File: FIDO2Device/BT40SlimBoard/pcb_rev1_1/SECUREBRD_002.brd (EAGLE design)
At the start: 30 x 30 mm, 37 parts, among them CN1 USB4105-GF-A, CN2 IF_5PIN_H, CN3 IF_2PIN_SOL, SW1 SKRPACE010, SW2 SKTADAE010, U1 BT40, U2 ADP122ACPZ-3.3-R7, U3 RV-3028-C7

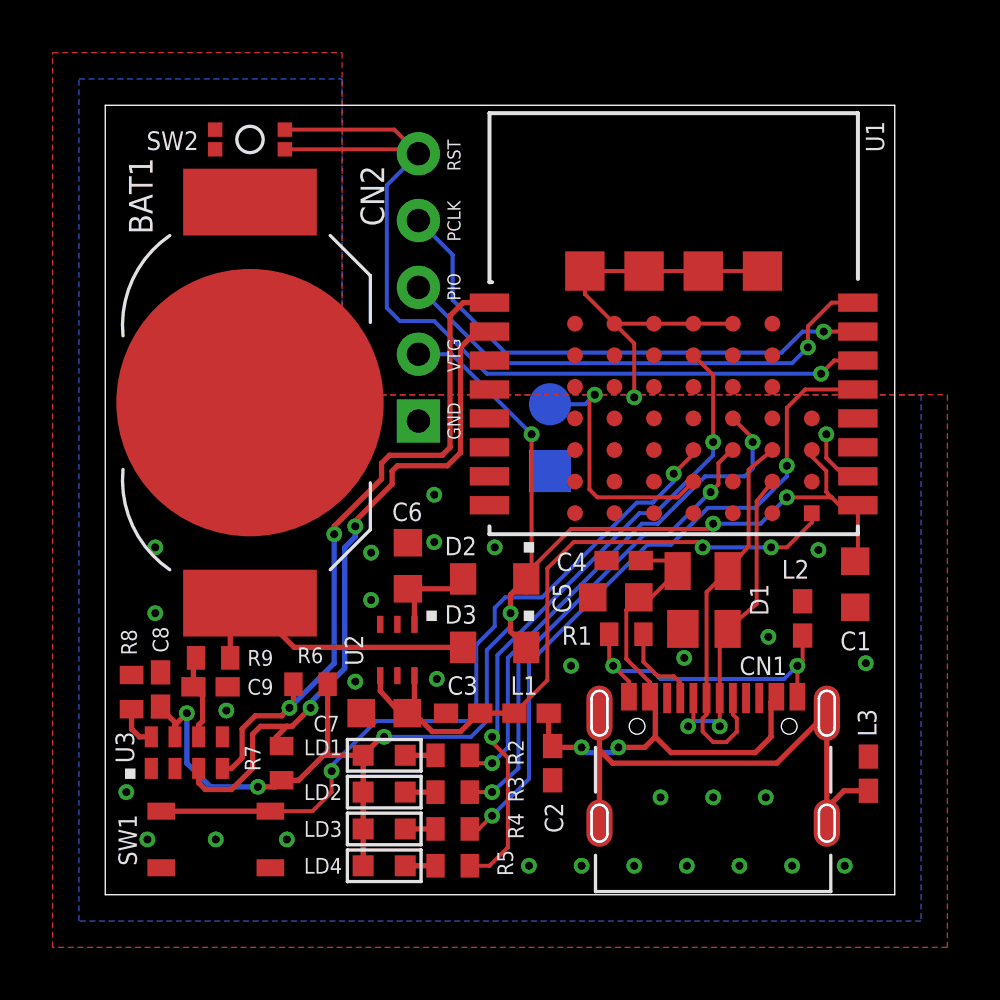
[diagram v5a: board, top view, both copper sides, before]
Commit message: 配線レイアウトを修正
・電池ホルダーの位置を微調整
・実装図面を修正
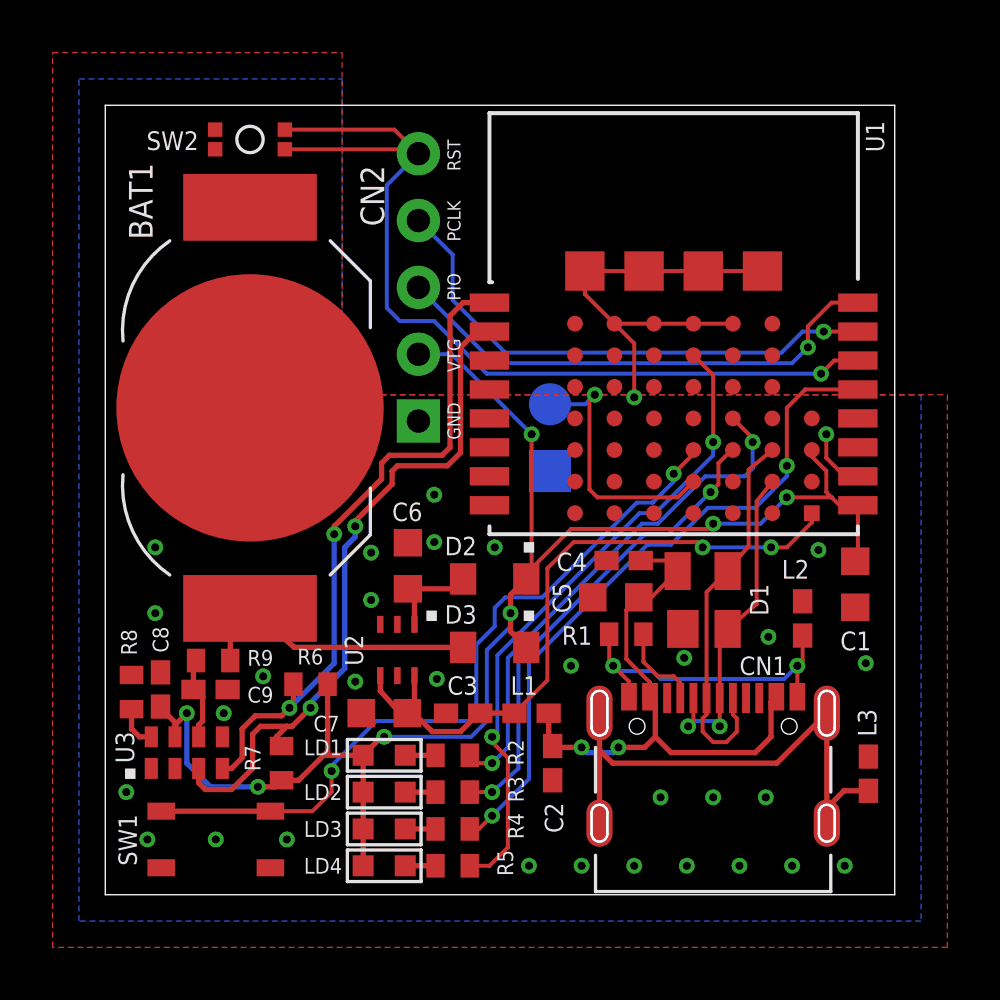
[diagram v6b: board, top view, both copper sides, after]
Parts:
- moved BAT1 0.20 mm to (5.50, 18.5)
- moved C9 0.10 mm to (4.00, 7.80)
- moved R9 0.10 mm to (4.10, 8.90)
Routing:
- net 0V: vias 31 -> 32
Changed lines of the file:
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@@
 <text x="15.8" y="18.6" size="0.6" layer="22" rot="MR270" align="bottom-center">TXD</text>
 <text x="15.8" y="16.1" size="0.6" layer="22" rot="MR270" align="bottom-center">GND</text>
+<dimension x1="0" y1="30" x2="30" y2="30" x3="15" y3="31.5" textsize="1.778" layer="51"/>
+<dimension x1="0" y1="0" x2="0" y2="30" x3="-1.5" y3="15" textsize="1.778" layer="51"/>
 </plain>
 <attributes>
@@
 <attribute name="VALUE" x="15.96125" y="11.04625" size="0.7112" layer="27" rot="R180" align="top-left"/>
 </element>
-<element name="BAT1" library="Connectors" package="BAT-HLD-012-SMT" value="BAT-HLD-012-SMT" x="5.5" y="18.7" smashed="yes" rot="R270">
-<attribute name="NAME" x="1.8" y="25.1" size="0.9" layer="25" rot="R90"/>
-<attribute name="VALUE" x="6.29" y="8.87" size="0.7" layer="27" rot="R270"/>
+<element name="BAT1" library="Connectors" package="BAT-HLD-012-SMT" value="BAT-HLD-012-SMT" x="5.5" y="18.5" smashed="yes" rot="R270">
+<attribute name="NAME" x="1.8" y="24.9" size="0.9" layer="25" rot="R90"/>
+<attribute name="VALUE" x="6.29" y="8.67" size="0.7" layer="27" rot="R270"/>
 </element>
 <element name="R1" library="Parts" package="R0402" value="5.1k" x="19.8" y="9.9" smashed="yes">
@@
 </element>
 <element name="R6" library="Parts" package="R0402" value="10k" x="7.8" y="8" smashed="yes">
-<attribute name="NAME" x="7.3" y="8.8" size="0.6" layer="25"/>
+<attribute name="NAME" x="7.3" y="8.75" size="0.6" layer="25"/>
 <attribute name="VALUE" x="7.244375" y="6.57125" size="0.7112" layer="27"/>
 </element>
@@
 <attribute name="VALUE" x="3.470625" y="6.585625" size="0.7112" layer="27" rot="R90"/>
 </element>
-<element name="C9" library="Parts" package="C0402K" value="0.1uF" x="4" y="7.9" smashed="yes">
-<attribute name="NAME" x="5.4" y="7.6" size="0.6" layer="25"/>
-<attribute name="VALUE" x="2.785625" y="6.529375" size="0.7112" layer="27"/>
-</element>
-<element name="R9" library="Parts" package="R0402" value="390" x="4.1" y="9" smashed="yes">
+<element name="C9" library="Parts" package="C0402K" value="0.1uF" x="4" y="7.8" smashed="yes">
+<attribute name="NAME" x="5.4" y="7.3" size="0.6" layer="25"/>
+<attribute name="VALUE" x="2.785625" y="6.429375" size="0.7112" layer="27"/>
+</element>
+<element name="R9" library="Parts" package="R0402" value="390" x="4.1" y="8.9" smashed="yes">
 <attribute name="NAME" x="5.4" y="8.7" size="0.6" layer="25"/>
-<attribute name="VALUE" x="3.544375" y="7.57125" size="0.7112" layer="27"/>
+<attribute name="VALUE" x="3.544375" y="7.47125" size="0.7112" layer="27"/>
 </element>
 </elements>
@@
 <contactref element="C9" pad="2"/>
 <contactref element="C8" pad="2"/>
-<via x="4.6" y="7" extent="1-16" drill="0.3048"/>
 <via x="0.8" y="3.9" extent="1-16" drill="0.3048"/>
 <via x="6.9" y="2.1" extent="1-16" drill="0.3048"/>
@@
 <via x="9.5" y="8.1" extent="1-16" drill="0.3048"/>
 <via x="10.1" y="13" extent="1-16" drill="0.3048"/>
+<via x="4.5" y="6.9" extent="1-16" drill="0.3048"/>
+<via x="6" y="8.3" extent="1-16" drill="0.3048"/>
 </signal>
 <signal name="VBUS_NRF">
@@
 <wire x1="3.55" y1="6.45" x2="3.7" y2="6.6" width="0.2032" layer="1"/>
 <wire x1="3.7" y1="6.6" x2="3.7" y2="7.55" width="0.2032" layer="1"/>
-<wire x1="3.7" y1="7.55" x2="3.35" y2="7.9" width="0.2032" layer="1"/>
-<wire x1="3.35" y1="7.9" x2="3.35" y2="8.9" width="0.2032" layer="1"/>
-<wire x1="3.35" y1="8.9" x2="3.45" y2="9" width="0.2032" layer="1"/>
+<wire x1="3.7" y1="7.55" x2="3.35" y2="7.8" width="0.2032" layer="1"/>
+<wire x1="3.35" y1="7.8" x2="3.35" y2="8.9" width="0.2032" layer="1"/>
+<wire x1="3.35" y1="8.9" x2="3.45" y2="8.9" width="0.2032" layer="1"/>
 </signal>
 <signal name="VDD_BAT">
@@
 <contactref element="BAT1" pad="+@2"/>
 <contactref element="D3" pad="A"/>
-<wire x1="4.75" y1="9" x2="4.75" y2="10.33" width="0.2032" layer="1"/>
-<wire x1="4.75" y1="10.33" x2="5.5" y2="11.08" width="0.2032" layer="1"/>
+<wire x1="4.75" y1="8.9" x2="4.75" y2="10.33" width="0.2032" layer="1"/>
+<wire x1="4.75" y1="10.33" x2="5.5" y2="10.88" width="0.2032" layer="1"/>
 <wire x1="13.6" y1="9.4" x2="7.18" y2="9.4" width="0.2032" layer="1"/>
-<wire x1="7.18" y1="9.4" x2="5.5" y2="11.08" width="0.2032" layer="1"/>
+<wire x1="7.18" y1="9.4" x2="5.5" y2="10.88" width="0.2032" layer="1"/>
 </signal>
 </signals>

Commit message: 配線レイアウトを修正
・プログラム用のスルーホール群を、基板右上部に移設
・基板裏側のTXDパッドを撤去
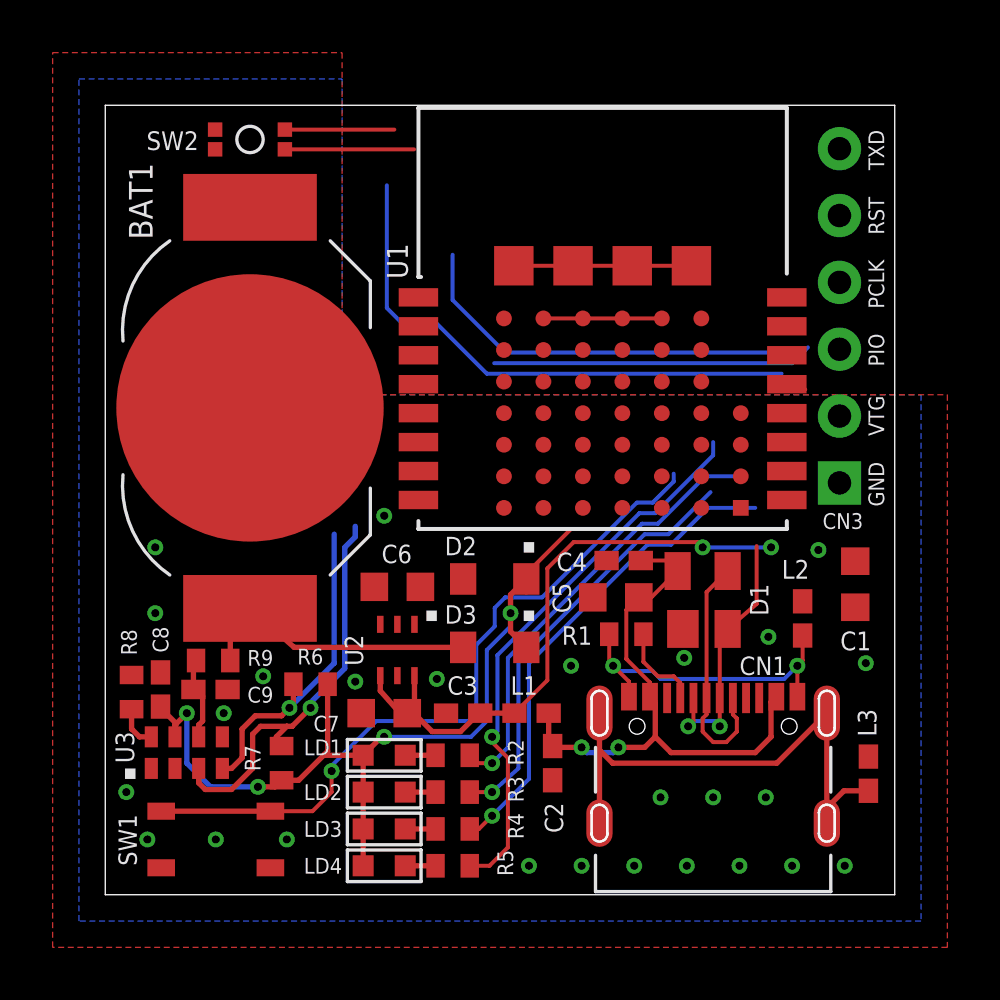
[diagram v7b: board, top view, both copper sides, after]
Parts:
- removed CN2: IF_5PIN_H, Connectors:HEADER_5PIN
- CN3: value IF_2PIN_SOL -> IF_6PIN; device Connectors:SOLPAD_2PIN -> Connectors:HEADER_6PIN
- moved CN3 12.5 mm to (27.9, 22.0), flipped to the top
- moved U1 2.71 mm to (11.9, 13.9)
- moved C6 0.89 mm to (11.1, 11.7), turned to 180 degrees
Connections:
- net 0V: no longer CN2.1
- net RESET: now also CN3.5; no longer CN2.5
- net SWCLK: now also CN3.4; no longer CN2.4
- net SWDIO: now also CN3.3; no longer CN2.3
- net TXD: now also CN3.6; no longer CN3.2
- net VDD_NRF: now also CN3.2; no longer CN2.2
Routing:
- net VDD_NRF: track 61.6 -> 35.1 mm, vias 7 -> 4
- net SDA: track 25.4 -> 12.4 mm, vias 2 -> 1
- net SCL: track 26.4 -> 15.5 mm, vias 2 -> 1
- net TXD: track 9.85 -> 0.00 mm, vias 1 -> 0
- net 0V: track 19.2 -> 11.2 mm, vias 32 -> 26
- net SWDIO: track 19.3 -> 12.2 mm, vias 1 -> 0
- net LED3: track 25.8 -> 19.2 mm, vias 2 -> 1
- net RESET: track 36.1 -> 29.8 mm, vias 1 -> 0
- net D_P: track 14.8 -> 9.46 mm
- net SWCLK: track 20.1 -> 15.0 mm, vias 1 -> 0
- net N$3: track 3.71 -> 0.00 mm
- net LED4: track 24.8 -> 21.2 mm, vias 2 -> 1
- net LED1: track 19.8 -> 17.1 mm, vias 2 -> 1
- net D_N: track 12.7 -> 10.0 mm
- net VBUS_NRF: track 25.4 -> 23.1 mm
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
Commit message: 配線レイアウトを修正
・SWD、RESET、I2Cの配線レイアウトを変更
・一部の部品について、配置を調整
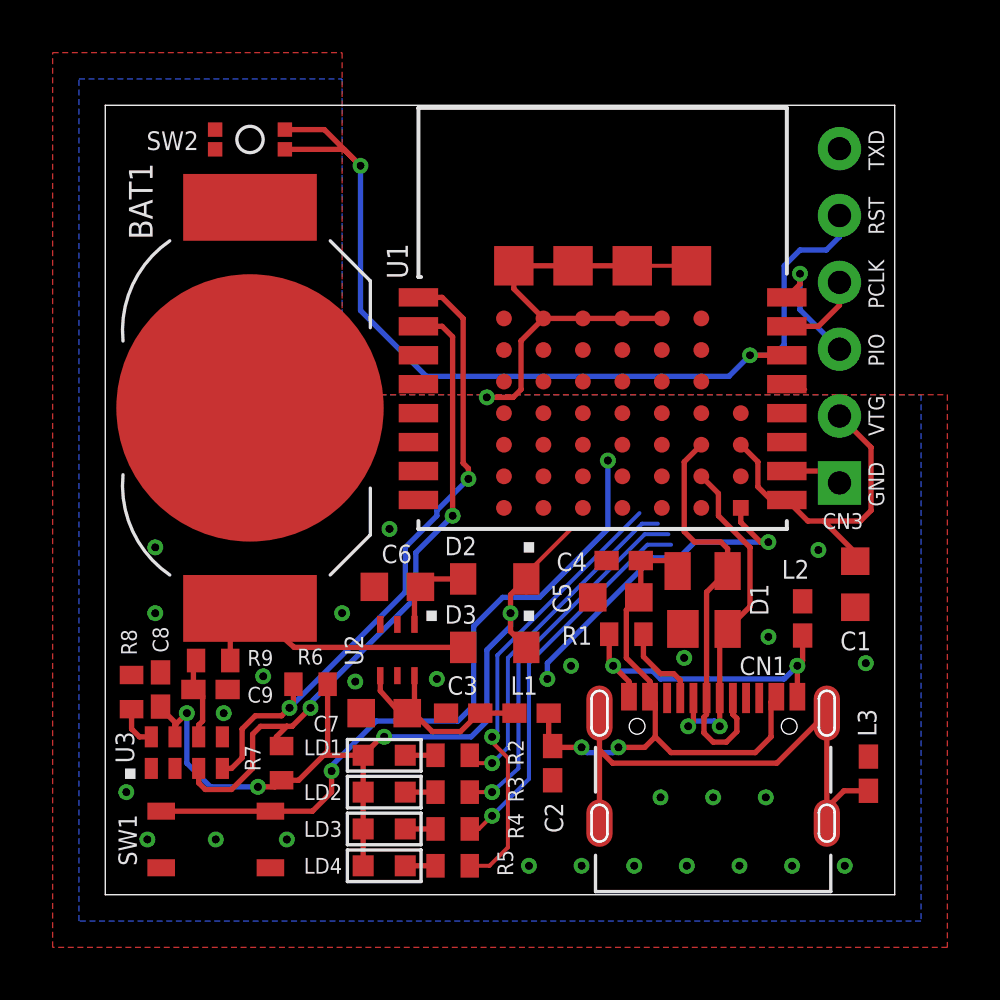
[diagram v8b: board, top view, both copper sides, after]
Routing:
- net VDD_NRF: track 35.1 -> 48.0 mm
- net SDA: track 12.4 -> 24.8 mm, vias 1 -> 2
- net SWCLK: track 15.0 -> 3.20 mm
- net SCL: track 15.5 -> 25.7 mm, vias 1 -> 2
- net 0V: track 11.2 -> 20.4 mm, vias 26 -> 28
- net RESET: track 29.8 -> 37.5 mm, vias 0 -> 2
- net SWDIO: track 12.2 -> 4.60 mm, vias 0 -> 1
- net D_P: track 9.46 -> 15.8 mm
- net LED4: track 21.2 -> 17.0 mm
- net LED1: track 17.1 -> 13.0 mm
- net LED3: track 19.2 -> 15.4 mm
- net N$3: track 0.00 -> 3.27 mm
- net D_N: track 10.0 -> 13.3 mm
- net LED2: track 16.2 -> 14.0 mm
- net VBUS_NRF: track 23.1 -> 20.9 mm
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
